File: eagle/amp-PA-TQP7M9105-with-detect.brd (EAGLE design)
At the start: 44 x 26 mm, 46 parts, among them J1 142-0701-851, J2 142-0701-851, Q1 P-CH, Q2 N-CH, U1 TQP7M9105, U2 BDCN-20-13+, U3 LT5534, U4 LT5534

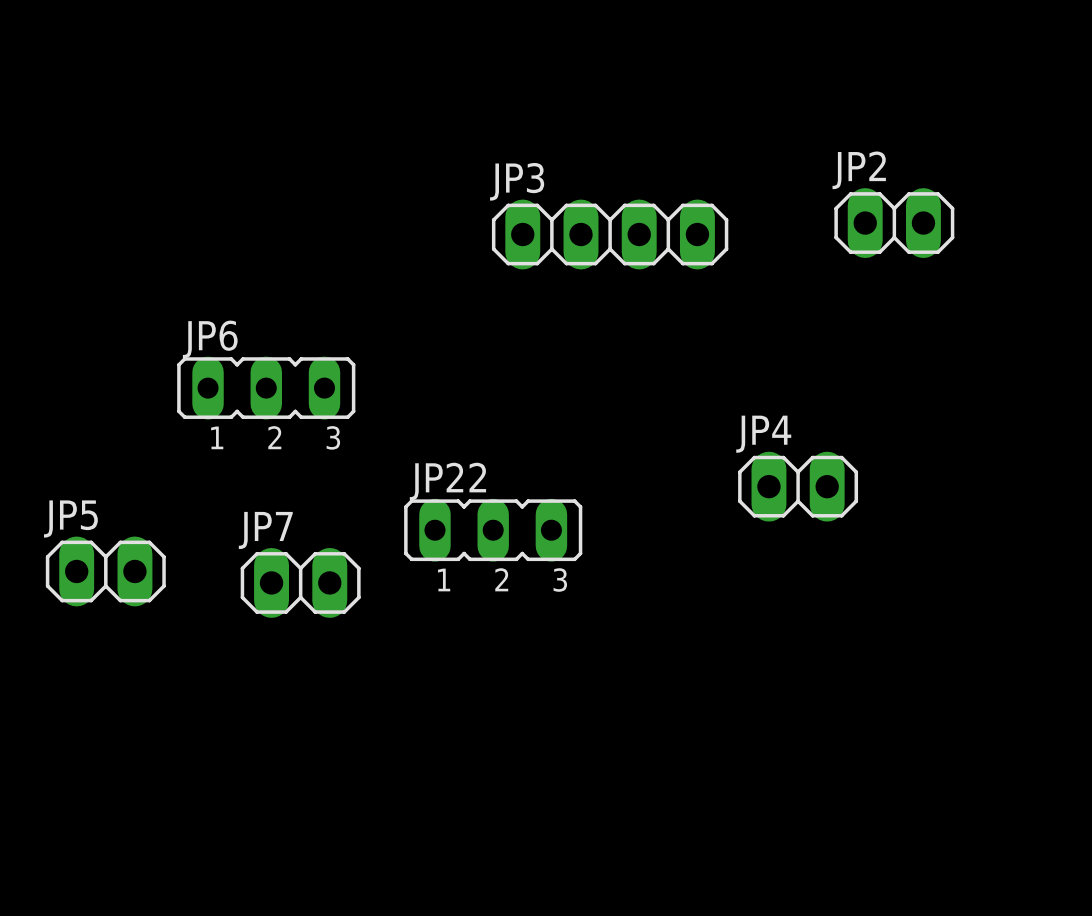
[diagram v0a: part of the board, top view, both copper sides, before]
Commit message: Update PA TQP7M9105 schematic
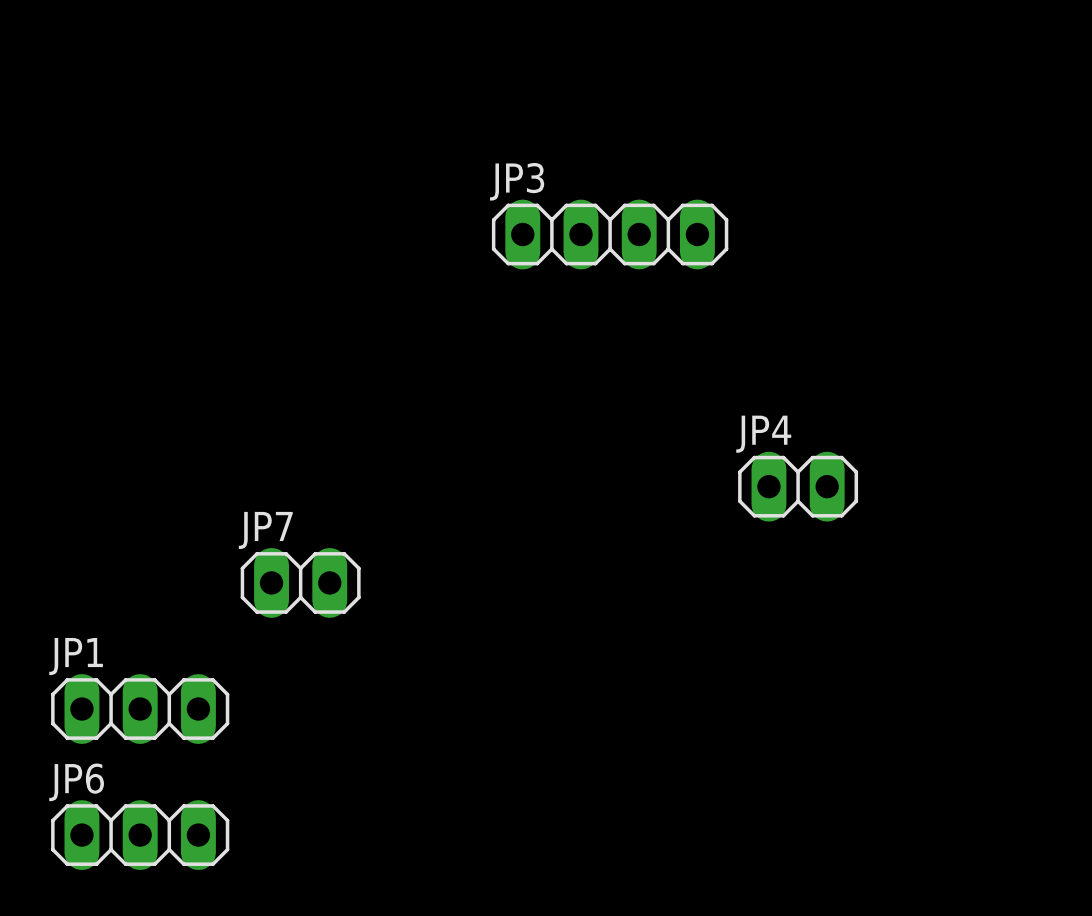
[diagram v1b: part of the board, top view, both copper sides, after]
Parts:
- removed JP2, JP5: (no value), pinhead:1X02
- removed JP22: (no value), jumper:JP2
- added JP1: (no value), pinhead:1X03
- JP6: device jumper:JP2 -> pinhead:1X03
- moved JP6 20.3 mm to (-11.0, -46.5)
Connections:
- removed net N$11: JP2.2, JP22.1
- removed net N$25 (its old number): JP5.2, JP6.1
- net +3V3: now also JP1.1, JP6.1; no longer JP22.3, JP6.3
- net GND: now also JP1.3, JP6.3; no longer JP2.1, JP5.1
- net N$10: now also JP1.2; no longer JP22.2

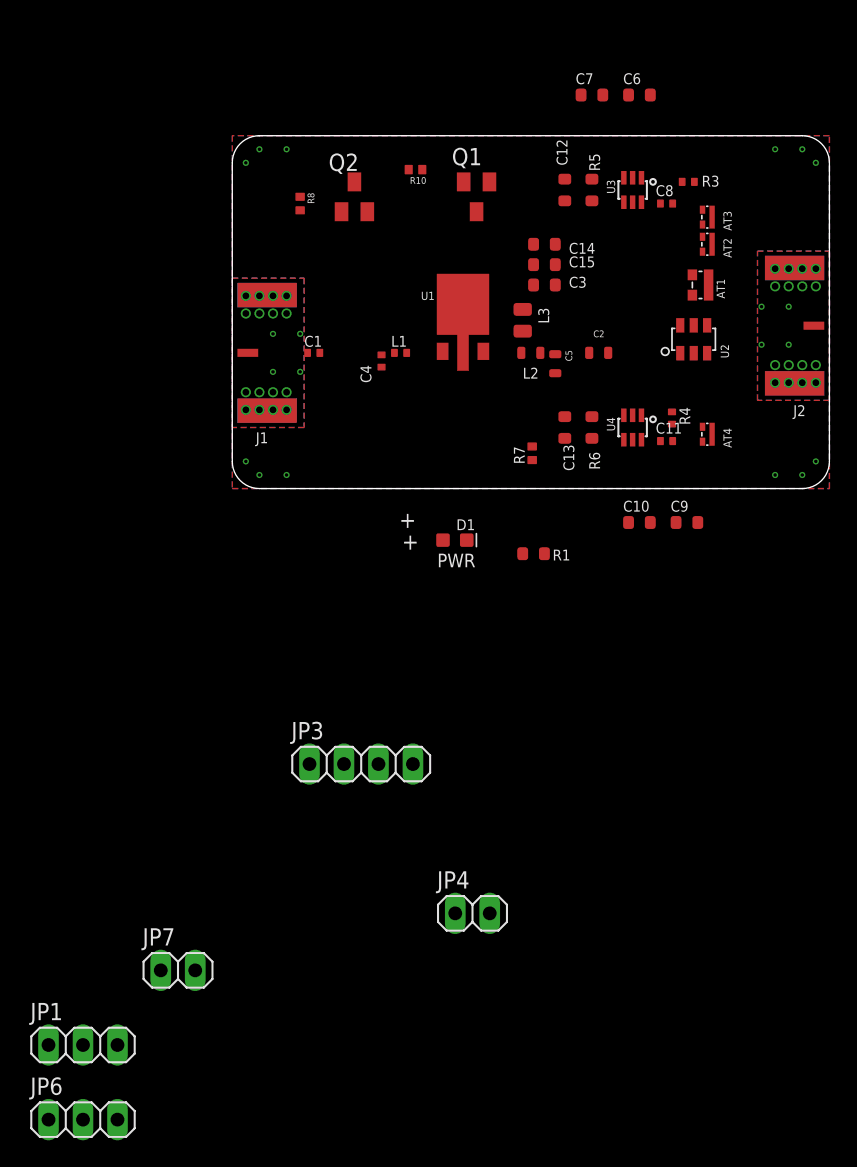
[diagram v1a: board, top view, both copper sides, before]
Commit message: Update PA layout placement
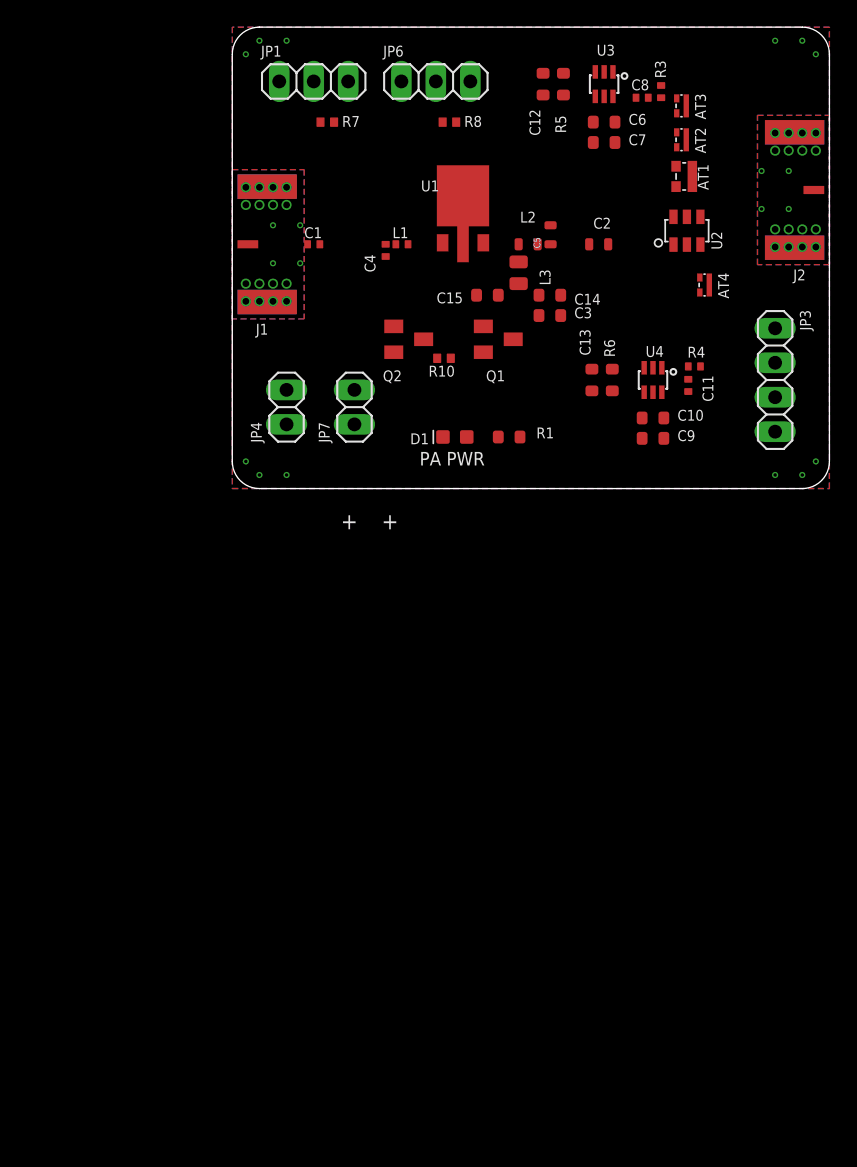
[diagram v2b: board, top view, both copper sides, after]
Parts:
- C3: value DNP -> 1u
- moved JP6 80.8 mm to (15.0, 30.0)
- moved JP1 73.0 mm to (6.00, 30.0)
- moved JP7 43.5 mm to (9.00, 6.00), turned to 90 degrees
- moved JP3 41.6 mm to (40.0, 8.00), turned to 270 degrees
- moved JP4 39.7 mm to (4.00, 6.00), turned to 90 degrees
- moved R7 28.7 mm to (7.00, 27.0), turned to 180 degrees
- moved R10 14.1 mm to (15.6, 9.60)
- moved R8 12.5 mm to (16.0, 27.0), turned to 180 degrees
- moved Q2 11.2 mm to (13.0, 11.0), turned to 270 degrees
- moved AT4 11.0 mm to (34.8, 15.0)
- moved Q1 10.6 mm to (19.6, 11.0), turned to 270 degrees
- moved J2 10.0 mm to (44.0, 22.0)
- moved C5 9.51 mm to (23.4, 18.7), turned to 90 degrees
- moved R1 8.79 mm to (20.4, 3.80)
- moved AT3 8.42 mm to (33.1, 28.2)
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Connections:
- net N$14 renamed FWD
- net N$15 renamed REV
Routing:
- added copper zone on layer 15, net +3V3
- removed copper zone on layer 15, net GND
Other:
- board size 44 x 26 mm -> 44 x 34 mm
- board text added: "PA PWR"
- board text added: "UHF 1W Power Amplifier 436.5 MHz - TQP7M9105 PSAS / OreSat 2020-07-30 v1.0 E.M. KJ7AOG"
- board text removed: "PWR"
- board text removed: "UHF PA TQP7M9105 PSAS / OreSat 2020-07-28 v1.0 E.M. KJ7AOG"

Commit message: Update PA TQP7M9105 layout
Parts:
- removed JP7: (no value), pinhead:1X02
- added JP5: (no value), pinhead:1X04
- JP3: device pinhead:1X04 -> pinhead:1X02
- moved JP3 31.1 mm to (9.00, 6.00), turned to 90 degrees
- moved Q2 3.42 mm to (16.4, 10.6), turned to 180 degrees
- moved R10 2.20 mm to (13.4, 9.60), turned to 90 degrees
- moved C15 0.94 mm to (19.6, 13.8)
- moved C14 0.94 mm to (22.6, 13.8)
- moved C3 0.94 mm to (22.6, 12.2)
- moved Q1 0.85 mm to (20.4, 10.6), turned to 0 degrees
- moved R7 0.60 mm to (7.00, 26.4)
- moved R8 0.60 mm to (16.0, 26.4)
- moved AT3 0.22 mm to (33.0, 28.0)
- moved C6 0.20 mm to (27.6, 27.0)
- moved C7 0.20 mm to (27.6, 25.5)
- moved C10 0.20 mm to (31.2, 5.20)
- moved C9 0.20 mm to (31.2, 3.70)
- moved AT1 0.20 mm to (33.1, 23.0)
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- renumbered JP6 to JP2
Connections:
- net N$19 renamed CAPS
- net +5V: now also JP3.2; no longer JP7.2
- net FWD: now also JP5.1; no longer JP3.1
- net GND: now also JP3.1, JP5.2, JP5.4; no longer JP3.2, JP3.4, JP7.1
- net REV: now also JP5.3; no longer JP3.3
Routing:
- net GND: track 0.00 -> 59.6 mm, vias 52 -> 220
- net N$10: track 0.00 -> 58.0 mm, vias 0 -> 2
- net FWD: track 0.00 -> 26.9 mm, vias 0 -> 1
- net N$25: track 0.00 -> 25.6 mm, vias 0 -> 1
- net REV: track 0.00 -> 19.6 mm
- net +3V3: track 0.00 -> 13.8 mm, vias 0 -> 4
- net CAPS: track 0.00 -> 9.69 mm
- net N$7: track 0.00 -> 8.76 mm
- net N$13: track 0.00 -> 6.57 mm
- net N$23: track 0.00 -> 6.25 mm
- net +5V: track 0.00 -> 5.92 mm
- net N$3: track 0.00 -> 5.60 mm
- net N$2: track 0.00 -> 4.82 mm
- net N$1: track 0.00 -> 4.40 mm
- net N$5: track 0.00 -> 3.95 mm
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- added copper zone on layer 1, net +5V
- added copper zone on layer 1, net CAPS
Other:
- board text added: "+3V3"
- board text added: "+5V"
- board text added: "-"
- board text added: "FWD"
- board text added: "IN"
- board text added: "Log Amps EN"
- board text added: "Log Amps Out"
- board text added: "OUT"
- board text added: "PA Enable"
- board text added: "REV"
- board text added: "UHF 1W Power Amplifier 436.5 MHz - TQP7M9105 PSAS / OreSat 2020-07-31 v1.0 E.M. KJ7AOG"
- board text removed: "UHF 1W Power Amplifier 436.5 MHz - TQP7M9105 PSAS / OreSat 2020-07-30 v1.0 E.M. KJ7AOG"

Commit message: Update UHF PA board
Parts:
- added JP6: NP, oresat-rcl:.0603-B-NOSILK
- added R9: 0, oresat-rcl:.0603-B-NOSILK
- moved R7 2.91 mm to (4.20, 25.6), turned to 0 degrees
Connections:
- removed net N$10: JP1.2, R7.2, U3.1, U4.1
- new net N$11: JP1.2, R7.2, R9.2
- new net N$14: JP6.2, R9.1, U3.1, U4.1
- net N$25: now also JP6.1
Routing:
- net N$10: track 58.0 -> 0.00 mm, vias 2 -> 0
- net N$14: track 0.00 -> 54.6 mm, vias 0 -> 3
- net N$11: track 0.00 -> 6.70 mm
- net N$25: track 25.6 -> 27.4 mm, vias 1 -> 2
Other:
- board text added: "1"
- board text added: "2"
- board text added: "HOT"
- board text added: "UHF 1W Power Amplifier 436.5 MHz - TQP7M9105 PSAS / OreSat 2020-08-01 v1.0 E.M. KJ7AOG"
- board text removed: "UHF 1W Power Amplifier 436.5 MHz - TQP7M9105 PSAS / OreSat 2020-07-31 v1.0 E.M. KJ7AOG"
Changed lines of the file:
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@@
 <layer number="27" name="tValues" color="7" fill="1" visible="yes" active="yes"/>
 <layer number="28" name="bValues" color="7" fill="1" visible="yes" active="yes"/>
-<layer number="29" name="tStop" color="7" fill="3" visible="yes" active="yes"/>
-<layer number="30" name="bStop" color="7" fill="6" visible="yes" active="yes"/>
+<layer number="29" name="tStop" color="7" fill="3" visible="no" active="yes"/>
+<layer number="30" name="bStop" color="7" fill="6" visible="no" active="yes"/>
 <layer number="31" name="tCream" color="7" fill="4" visible="no" active="yes"/>
 <layer number="32" name="bCream" color="7" fill="5" visible="no" active="yes"/>
@@
 436.5 MHz - TQP7M9105
 PSAS / OreSat
-2020-07-31  v1.0
+2020-08-01  v1.0
 E.M.  KJ7AOG</text>
 <text x="14" y="1.7" size="1" layer="21" font="vector" ratio="15">PA PWR</text>
@@
 <wire x1="32.6" y1="25" x2="32.4" y2="23.8" width="1.6" layer="29"/>
 <wire x1="32.4" y1="23.8" x2="32.4" y2="21.6" width="1.6" layer="29"/>
+<wire x1="20" y1="19.2" x2="20" y2="25.2" width="0.2" layer="21" style="shortdash"/>
+<wire x1="20" y1="25.2" x2="14" y2="25.2" width="0.2" layer="21" style="shortdash"/>
+<wire x1="14" y1="25.2" x2="14" y2="19.2" width="0.2" layer="21" style="shortdash"/>
+<text x="14.8" y="22.2" size="2" layer="21" font="vector" ratio="15">HOT</text>
+<text x="5.75" y="25.4" size="0.6" layer="21" font="vector" ratio="15">1</text>
+<text x="11.1" y="25.4" size="0.6" layer="21" font="vector" ratio="15">2</text>
+<wire x1="6.2" y1="26.4" x2="11" y2="26.4" width="0.1" layer="21"/>
+<wire x1="11" y1="26.4" x2="11" y2="24.8" width="0.1" layer="21"/>
+<wire x1="11" y1="24.8" x2="6.2" y2="24.8" width="0.1" layer="21"/>
+<wire x1="6.2" y1="24.8" x2="6.2" y2="26.4" width="0.1" layer="21"/>
 </plain>
 <attributes>
@@
 </element>
 <element name="U1" library="U-Qorvo-TQP7M9105-PA" package="TQP7M9105" value="TQP7M9105" x="17" y="18" smashed="yes">
-<attribute name="NAME" x="13.1" y="19.9" size="0.8" layer="25" font="vector" ratio="15"/>
+<attribute name="NAME" x="12.7" y="20.7" size="0.8" layer="25" font="vector" ratio="15"/>
 </element>
 <element name="U2" library="U-MiniCirc-BDCN-20-13+-coupler" package="BDCN-20-13+" value="BDCN-20-13+" x="33.5" y="19" smashed="yes">
@@
 <attribute name="NAME" x="26.5" y="8" size="0.3" layer="33" ratio="15" rot="R90" align="center"/>
 </element>
-<element name="R7" library="oresat-rcl" package=".0402-B-NOSILK" value="33k" x="7" y="26.4" smashed="yes" rot="R180">
-<attribute name="NAME" x="7.6" y="25.85" size="0.8" layer="25" font="vector" ratio="15" rot="R180"/>
-<attribute name="NAME" x="7" y="26.4" size="0.2" layer="33" ratio="15" rot="R180" align="center"/>
+<element name="R7" library="oresat-rcl" package=".0402-B-NOSILK" value="33k" x="4.2" y="25.6" smashed="yes">
+<attribute name="NAME" x="3.6" y="24.15" size="0.8" layer="25" font="vector" ratio="15"/>
+<attribute name="NAME" x="4.2" y="25.6" size="0.2" layer="33" ratio="15" align="center"/>
 </element>
 <element name="Q1" library="transistor-small-signal" library_urn="urn:adsk.eagle:library:401" package="SOT23" package3d_urn="urn:adsk.eagle:package:28738/2" value="P-CH" x="20.35" y="10.6" smashed="yes">
@@
 </element>
 <element name="R8" library="oresat-rcl" package=".0402-B-NOSILK" value="33k" x="16" y="26.4" smashed="yes" rot="R180">
-<attribute name="NAME" x="16.6" y="25.85" size="0.8" layer="25" font="vector" ratio="15" rot="R180"/>
+<attribute name="NAME" x="19" y="26.65" size="0.8" layer="25" font="vector" ratio="15" rot="R180"/>
 <attribute name="NAME" x="16" y="26.4" size="0.2" layer="33" ratio="15" rot="R180" align="center"/>
 </element>
@@
 <attribute name="POPULARITY" value="92" x="15" y="30" size="1.778" layer="27" display="off"/>
 <attribute name="VALUE" x="11.19" y="26.825" size="1.27" layer="27"/>
+</element>
+<element name="JP6" library="oresat-rcl" package=".0603-B-NOSILK" value="NP" x="9.4" y="25.6" smashed="yes" rot="R180">
+<attribute name="NAME" x="9.4" y="24.6" size="0.8" layer="25" font="vector" ratio="15" rot="R180"/>
+<attribute name="NAME" x="9.4" y="25.6" size="0.3" layer="33" ratio="15" rot="R180" align="center"/>
+</element>
+<element name="R9" library="oresat-rcl" package=".0603-B-NOSILK" value="0" x="7.8" y="25.6" smashed="yes" rot="R180">
+<attribute name="NAME" x="7.8" y="25.6" size="0.3" layer="33" ratio="15" rot="R180" align="center"/>
 </element>
 </elements>
@@
 <via x="23.45" y="20.2" extent="1-16" drill="0.5"/>
 <via x="11.3" y="16.35" extent="1-16" drill="0.5"/>
-<via x="8.3" y="26.4" extent="1-16" drill="0.5"/>
+<via x="2.9" y="25.6" extent="1-16" drill="0.5"/>
 <via x="17.3" y="26.4" extent="1-16" drill="0.5"/>
 <via x="29.4" y="27" extent="1-16" drill="0.5"/>
@@
 <wire x1="23.45" y1="19.4" x2="23.45" y2="20.2" width="0.6" layer="1"/>
 <wire x1="11.3" y1="17.1" x2="11.3" y2="16.35" width="0.5" layer="1"/>
-<wire x1="7.5" y1="26.4" x2="8.3" y2="26.4" width="0.6" layer="1"/>
+<wire x1="3.7" y1="25.6" x2="2.9" y2="25.6" width="0.6" layer="1"/>
 <wire x1="16.5" y1="26.4" x2="17.3" y2="26.4" width="0.6" layer="1"/>
 <wire x1="22.9" y1="30.6" x2="21.85" y2="30.6" width="0.6" layer="1"/>
@@
 <via x="29.6" y="7" extent="1-16" drill="0.3"/>
 <via x="29.75" y="9.7" extent="1-16" drill="0.3"/>
+<polygon width="0.5" layer="1" thermals="no">
+<vertex x="14" y="25.2"/>
+<vertex x="20" y="25.2"/>
+<vertex x="20" y="19.6"/>
+<vertex x="14" y="19.6"/>
+</polygon>
 </signal>
 <signal name="N$1" class="2">
@@
 <wire x1="31.6" y1="28.8" x2="30.65" y2="28.8" width="0.38" layer="1"/>
 </signal>
-<signal name="N$10">
-<contactref element="U3" pad="1"/>
-<contactref element="U4" pad="1"/>
-<contactref element="R7" pad="2"/>
-<contactref element="JP1" pad="2"/>
-<wire x1="6" y1="30" x2="6" y2="26.9" width="0.6" layer="1"/>
-<wire x1="6" y1="26.9" x2="6.5" y2="26.4" width="0.6" layer="1"/>
-<wire x1="31.65" y1="8.9" x2="31.65" y2="10.1" width="0.4" layer="1"/>
-<via x="31.65" y="10.1" extent="1-16" drill="0.35"/>
-<wire x1="31.65" y1="10.1" x2="31.65" y2="14.95" width="0.4" layer="16"/>
-<wire x1="31.65" y1="14.95" x2="20.6" y2="26" width="0.4" layer="16"/>
-<wire x1="20.6" y1="32.2" x2="20.6" y2="26" width="0.4" layer="16"/>
-<wire x1="28.05" y1="30.7" x2="28.05" y2="31.4" width="0.4" layer="1"/>
-<wire x1="28.05" y1="31.4" x2="28.15" y2="31.5" width="0.4" layer="1"/>
-<via x="28.15" y="31.5" extent="1-16" drill="0.3"/>
-<wire x1="28.15" y1="31.5" x2="28.2" y2="31.45" width="0.4" layer="16"/>
-<wire x1="28.2" y1="31.45" x2="28.2" y2="30.6" width="0.4" layer="16"/>
-<wire x1="25" y1="30.6" x2="23.4" y2="32.2" width="0.4" layer="16"/>
-<wire x1="23.4" y1="32.2" x2="20.6" y2="32.2" width="0.4" layer="16"/>
-<wire x1="28.2" y1="30.6" x2="25" y2="30.6" width="0.4" layer="16"/>
-<wire x1="20.6" y1="32.2" x2="6.8" y2="32.2" width="0.4" layer="16"/>
-<wire x1="6.8" y1="32.2" x2="6" y2="31.4" width="0.4" layer="16"/>
-<wire x1="6" y1="31.4" x2="6" y2="30" width="0.4" layer="16"/>
-</signal>
 <signal name="N$12" class="1">
 <contactref element="C11" pad="1"/>
@@
 <via x="17" y="12.8" extent="1-16" drill="0.35"/>
 <wire x1="17" y1="12.8" x2="12" y2="17.8" width="0.6" layer="16"/>
-<wire x1="12" y1="17.8" x2="12" y2="26" width="0.6" layer="16"/>
+<wire x1="12" y1="17.8" x2="12" y2="25.6" width="0.6" layer="16"/>
+<wire x1="12" y1="25.6" x2="12" y2="26" width="0.6" layer="16"/>
 <wire x1="12" y1="26" x2="15" y2="29" width="0.6" layer="16"/>
 <wire x1="15" y1="29" x2="15" y2="30" width="0.6" layer="16"/>
+<contactref element="JP6" pad="1"/>
+<wire x1="10.2" y1="25.6" x2="12" y2="25.6" width="0.4" layer="1"/>
+<via x="12" y="25.6" extent="1-16" drill="0.35"/>
+</signal>
+<signal name="N$11">
+<contactref element="JP1" pad="2"/>
+<contactref element="R9" pad="2"/>
+<contactref element="R7" pad="2"/>
+<wire x1="4.7" y1="25.6" x2="6" y2="25.6" width="0.4" layer="1"/>
+<wire x1="6" y1="25.6" x2="7" y2="25.6" width="0.4" layer="1"/>
+<wire x1="6" y1="30" x2="6" y2="25.6" width="0.4" layer="1"/>
+</signal>
+<signal name="N$14">
+<contactref element="JP6" pad="2"/>
+<contactref element="R9" pad="1"/>
+<contactref element="U3" pad="1"/>
+<contactref element="U4" pad="1"/>
+<wire x1="31.65" y1="8.9" x2="31.65" y2="10.1" width="0.4" layer="1"/>
+<via x="31.65" y="10.1" extent="1-16" drill="0.35"/>
+<wire x1="31.65" y1="10.1" x2="31.65" y2="14.95" width="0.4" layer="16"/>
+<wire x1="31.65" y1="14.95" x2="20.6" y2="26" width="0.4" layer="16"/>
+<wire x1="20.6" y1="32.2" x2="20.6" y2="26" width="0.4" layer="16"/>
+<wire x1="28.05" y1="30.7" x2="28.05" y2="31.4" width="0.4" layer="1"/>
+<wire x1="28.05" y1="31.4" x2="28.15" y2="31.5" width="0.4" layer="1"/>
+<via x="28.15" y="31.5" extent="1-16" drill="0.3"/>
+<wire x1="28.15" y1="31.5" x2="28.2" y2="31.45" width="0.4" layer="16"/>
+<wire x1="28.2" y1="31.45" x2="28.2" y2="30.6" width="0.4" layer="16"/>
+<wire x1="25" y1="30.6" x2="23.4" y2="32.2" width="0.4" layer="16"/>
+<wire x1="23.4" y1="32.2" x2="20.6" y2="32.2" width="0.4" layer="16"/>
+<wire x1="28.2" y1="30.6" x2="25" y2="30.6" width="0.4" layer="16"/>
+<wire x1="11.8" y1="32.2" x2="10.6" y2="31" width="0.4" layer="16"/>
+<wire x1="10.6" y1="31" x2="10.6" y2="28.2" width="0.4" layer="16"/>
+<via x="10.6" y="28.2" extent="1-16" drill="0.35"/>
+<wire x1="10.6" y1="28.2" x2="8.6" y2="26.2" width="0.4" layer="1"/>
+<wire x1="8.6" y1="26.2" x2="8.6" y2="25.6" width="0.4" layer="1"/>
+<wire x1="20.6" y1="32.2" x2="11.8" y2="32.2" width="0.4" layer="16"/>
 </signal>
 </signals>
